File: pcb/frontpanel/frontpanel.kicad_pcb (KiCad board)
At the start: 4 copper layers, 90 parts, among them J1 PICOBLADE_10POS, J2 CONN_01X03, J3 XILINX_JTAG, U1 STM32L431VxIx, U2 TCA6424A

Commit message: Finished initial front panel schematic and design review
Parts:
- added C15: 4.7 uF, azonenberg_pcb:EIA_0603_CAP_NOSILK, F.Cu at (168.8, 51.4)
- added C16: 0.47 uF, azonenberg_pcb:EIA_0402_CAP_NOSILK, F.Cu at (171.7, 51.2)
- added C17: 0.47 uF, azonenberg_pcb:EIA_0402_CAP_NOSILK, F.Cu at (168.3, 53.0)
- added C18: 4.7 uF 25V, azonenberg_pcb:EIA_0805_CAP_NOSILK, F.Cu at (142.6, 62.4)
- added C19: 1 uF 25V, azonenberg_pcb:EIA_0805_CAP_NOSILK, F.Cu at (138.9, 62.4)
- added C20: 1 uF 25V, azonenberg_pcb:EIA_0805_CAP_NOSILK, F.Cu at (138.9, 67.5)
- added C21: 1 uF 25V, azonenberg_pcb:EIA_0805_CAP_NOSILK, F.Cu at (138.9, 65.0)
- added C22: 1 uF 25V, azonenberg_pcb:EIA_0805_CAP_NOSILK, F.Cu at (135.3, 62.4)
- added C23: 1 uF 25V, azonenberg_pcb:EIA_0805_CAP_NOSILK, F.Cu at (135.3, 65.0)
- added C24: 1 uF 25V, azonenberg_pcb:EIA_0805_CAP_NOSILK, F.Cu at (135.3, 67.5)
- added C25: 1 uF 25V, azonenberg_pcb:EIA_0805_CAP_NOSILK, F.Cu at (142.6, 65.0)
- added C26: 0.47 uF, azonenberg_pcb:EIA_0402_CAP_NOSILK, F.Cu at (147.0, 48.0)
- added D33: CTS05S30,L3F, azonenberg_pcb:SOD882, F.Cu at (190.7, 59.0)
- added D34: CTS05S30,L3F, azonenberg_pcb:SOD882, F.Cu at (181.2, 65.7)
- added D35: CTS05S30,L3F, azonenberg_pcb:SOD882, F.Cu at (178.8, 67.2)
- added J4: DISPLAY, azonenberg_pcb:CONN_FFC_0.5MM_1x24_HIROSE_FH34SRJ-24S-0.5SH(50), F.Cu at (108.8, 97.0)
- added L1: TFM322512ALMA100MTAA, azonenberg_pcb:EIA_1210_CAP_NOSILK, F.Cu at (174.9, 66.8)
- added M1: LOGO, azonenberg_pcb:LONGTHING-1200DPI, F.Cu at (169.4, 46.7)
- added M2: LOGO, w_logo:Logo_silk_WEEE_3.4x5mm, F.Cu at (190.2, 46.2)
- added M3: LOGO, w_logo:Logo_silk_OSHW_6x6mm, F.Cu at (186.2, 61.0)
- added M4: LOGO, w_logo:Logo_silk_ROHS_10x5.6mm, F.Cu at (177.8, 61.5)
- added MH1: SCREWHOLE, azonenberg_pcb:MECHANICAL_CLEARANCEHOLE_4_40, B.Cu at (26.0, 108.0)
- added MH2: SCREWHOLE, azonenberg_pcb:MECHANICAL_CLEARANCEHOLE_4_40, F.Cu at (206.0, 89.0)
- added MH3: SCREWHOLE, azonenberg_pcb:MECHANICAL_CLEARANCEHOLE_4_40, B.Cu at (26.0, 89.0)
- added MH4: SCREWHOLE, azonenberg_pcb:MECHANICAL_CLEARANCEHOLE_4_40, F.Cu at (206.0, 108.0)
- added Q1: SSM6N58NU, azonenberg_pcb:DFN_6_0.65MM_2x2MM_GDS, F.Cu at (165.4, 52.3)
- added R38: 0.47, azonenberg_pcb:EIA_0402_RES_NOSILK, F.Cu at (178.7, 65.6)
- added SW1: SWITCH, azonenberg_pcb:SWITCH_RAFI_MICON_5, F.Cu at (160.2, 63.2)
- added SW2: SWITCH, azonenberg_pcb:SWITCH_RAFI_MICON_5, F.Cu at (166.8, 63.2)
- added TP2: CONN_01X08, azonenberg_pcb:CONN_HEADER_2.54MM_1x8, B.Cu at (123.0, 92.0)
- added TP3: CONN_01X08, azonenberg_pcb:CONN_HEADER_2.54MM_1x8, F.Cu at (174.9, 39.6)
- added TP4: U.FL, azonenberg_pcb:CONN_U.FL_TE_1909763-1, F.Cu at (155.0, 43.0)
- added TP5: U.FL, azonenberg_pcb:CONN_U.FL_TE_1909763-1, F.Cu at (160.6, 43.0)
- added U3: AT30TS74_UDFN, azonenberg_pcb:DFN_8_0.5MM_2x3MM_TALL, F.Cu at (202.4, 34.1)
- J1: moved to B.Cu
- moved J1 137.4 mm to (216.0, 99.0), turned to 90 degrees
- moved D20 83.1 mm to (185.0, 109.0)
- moved D17 82.2 mm to (161.0, 109.0)
- moved D19 74.8 mm to (177.0, 109.0)
- moved D18 65.3 mm to (169.0, 109.0)
- moved D16 59.9 mm to (153.0, 109.0)
- moved D15 53.0 mm to (145.0, 109.0)
- moved D22 52.9 mm to (136.7, 35.8)
- moved D24 52.9 mm to (124.4, 53.2)
- moved TP1 52.9 mm to (126.6, 37.2)
- moved C1 52.9 mm to (148.3, 36.9)
- moved C10 52.9 mm to (134.8, 51.4)
- moved C12 52.9 mm to (104.0, 61.4)
- moved C13 52.9 mm to (143.0, 43.0)
- moved C14 52.9 mm to (138.0, 42.4)
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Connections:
- J3 pad 13: /GND -> unconnected-(J3-Pad13)
- U1 pad A1: unconnected-(U1-PadA1) -> /DIRIN_LED_3
- U1 pad A2: unconnected-(U1-PadA2) -> /DIRIN_LED_2
- U1 pad A6: unconnected-(U1-PadA6) -> /UART_TX
- U1 pad A7: unconnected-(U1-PadA7) -> /FRONTPANEL_MISO
- U1 pad B10: unconnected-(U1-PadB10) -> /DPY_SPI_DATA
- U1 pad B11: unconnected-(U1-PadB11) -> /DPY_SPI_SCK
- U1 pad B6: unconnected-(U1-PadB6) -> /UART_RX
- U1 pad D12: unconnected-(U1-PadD12) -> /DIROUT_LED_0
- U1 pad E12: unconnected-(U1-PadE12) -> /DIROUT_LED_1
- U1 pad H12: unconnected-(U1-PadH12) -> /DIROUT_LED_3
- U1 pad J12: unconnected-(U1-PadJ12) -> /DIROUT_LED_2
- U1 pad K12: unconnected-(U1-PadK12) -> /I2C_SCL
- U1 pad L11: unconnected-(U1-PadL11) -> /I2C_SDA
- U1 pad M10: unconnected-(U1-PadM10) -> /FRONTPANEL_SCK
- U1 pad M11: unconnected-(U1-PadM11) -> /DIRIN_LED_1
- U1 pad M12: unconnected-(U1-PadM12) -> /FRONTPANEL_MOSI
- U1 pad M2: unconnected-(U1-PadM2) -> /DPY_BS
- U1 pad M3: unconnected-(U1-PadM3) -> /DPY_SPI_CS_N
- U1 pad M4: unconnected-(U1-PadM4) -> /DPY_BUSY_N
- U1 pad M5: unconnected-(U1-PadM5) -> /FRONTPANEL_CS_N
- U1 pad M6: unconnected-(U1-PadM6) -> /DPY_RST_N
- U1 pad M7: unconnected-(U1-PadM7) -> /DPY_DC
- U1 pad M8: unconnected-(U1-PadM8) -> /TCA_RST_N
- U1 pad M9: unconnected-(U1-PadM9) -> /DIRIN_LED_0
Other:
- board outline added: 200 x 29 mm
- board text added: "Display body outline 59.20 x 29.20 mm"
- board text added: "Front panel has 31mm of height in play for holes etc Board is 29mm high so all good there Standard 5mm clearance from PCB edges should be fine"
- board text added: "MAX WIDTH of total board is 240 mm 225 preferred upper bound Target 200 for initial design with 25 for stretching if necessary"
- board text added: "Visible area 48.548 x 23.712 mm"

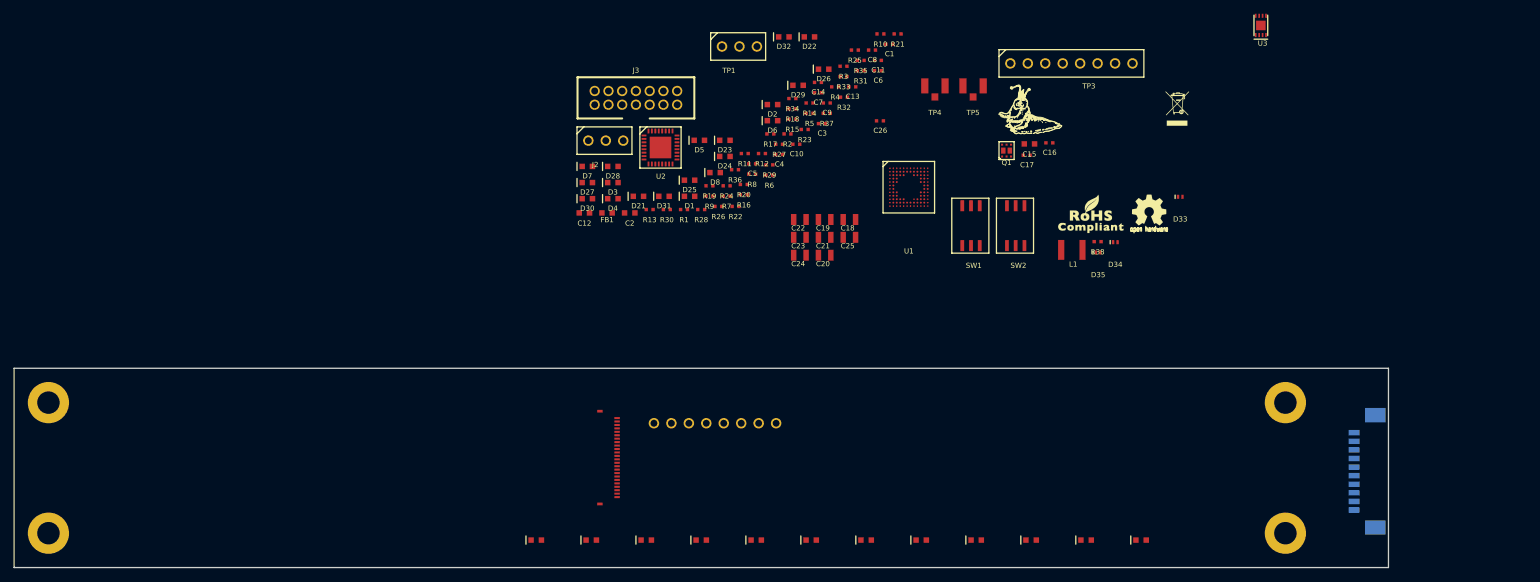
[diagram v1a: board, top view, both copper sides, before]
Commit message: Continued front panel PCB layout
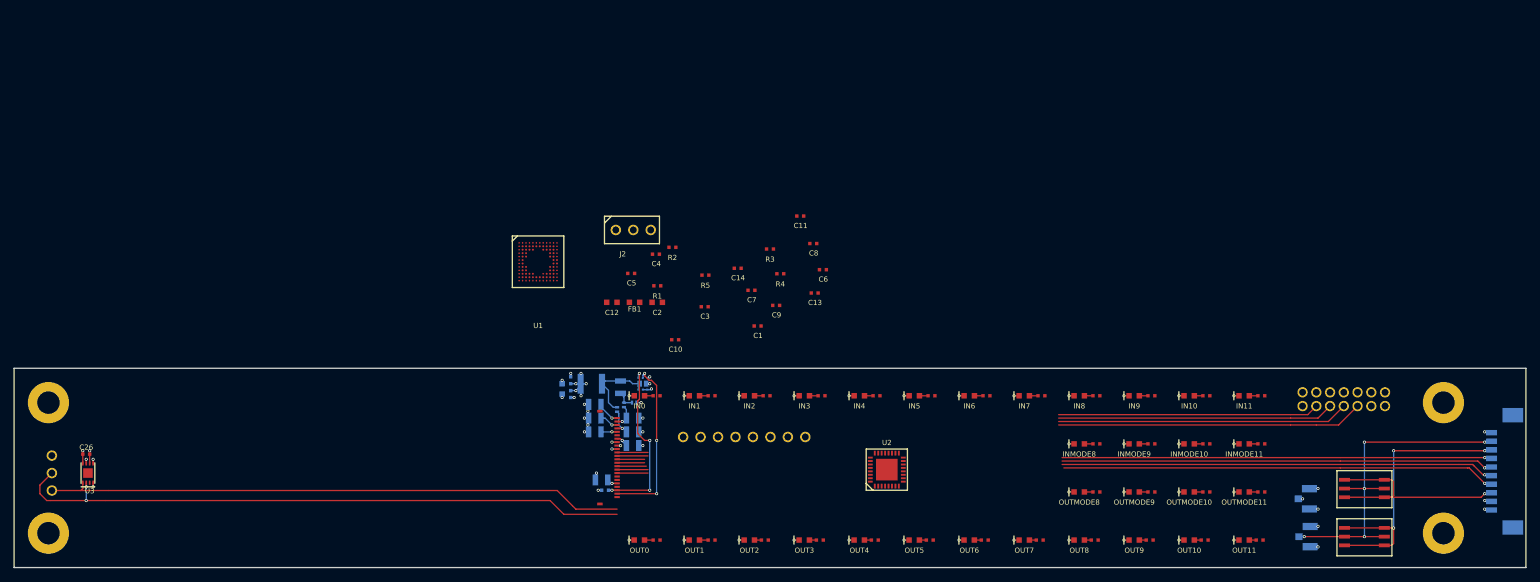
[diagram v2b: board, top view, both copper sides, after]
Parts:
- removed TP3: CONN_01X08, azonenberg_pcb:CONN_HEADER_2.54MM_1x8
- C15, C16, C17, C18, C19, C20, C21, C22, C23, C24, C25, D33, D34, D35, J3, L1, M1, M2, M3, M4, MH2, MH4, Q1, R38, TP1, TP4, TP5: moved to B.Cu
- moved U3 182.7 mm to (31.8, 99.2)
- moved C26 125.3 mm to (31.5, 96.5)
- moved TP1 117.7 mm to (26.5, 99.2), turned to 90 degrees
- moved J3 112.0 mm to (214.5, 88.5)
- moved D4 101.3 mm to (200.0, 102.0)
- moved D7 96.4 mm to (192.0, 95.0)
- moved R13 95.3 mm to (202.5, 95.0), turned to 180 degrees
- moved D3 95.2 mm to (192.0, 102.0)
- moved R25 92.5 mm to (202.2, 109.0), turned to 180 degrees
- moved R9 91.1 mm to (202.5, 102.0), turned to 180 degrees
- moved R24 86.6 mm to (194.2, 109.0), turned to 180 degrees
- moved D8 86.5 mm to (200.0, 95.0)
- moved D32 84.9 mm to (200.0, 88.0)
- moved D33 84.9 mm to (111.2, 89.0), turned to 180 degrees
- moved D30 84.6 mm to (184.0, 88.0)
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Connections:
- C22 pad 2: Net-(C22-Pad2) -> /GND
- C24 pad 2: Net-(C22-Pad2) -> /GND
- C25 pad 2: Net-(C22-Pad2) -> /GND
- TP1 pad 1: /I2C_SCL -> /I2C_SDA
- TP1 pad 2: /I2C_SDA -> /I2C_SCL
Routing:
- net /GND: track 0.00 -> 565.9 mm, vias 0 -> 60
- net /3V3: track 0.00 -> 288.2 mm, vias 0 -> 11
- net /3V3_SB: track 0.00 -> 152.2 mm, vias 0 -> 5
- net /I2C_SCL: track 0.00 -> 91.6 mm, vias 0 -> 2
- net /I2C_SDA: track 0.00 -> 84.6 mm
- net /FRONTPANEL_CS_N: track 0.00 -> 63.2 mm, vias 0 -> 1
- net /FRONTPANEL_MOSI: track 0.00 -> 63.2 mm, vias 0 -> 1
- net /FRONTPANEL_MISO: track 0.00 -> 63.0 mm, vias 0 -> 1
- net /FRONTPANEL_SCK: track 0.00 -> 62.6 mm, vias 0 -> 1
- net /JTAG_TDI: track 0.00 -> 44.6 mm
- net /JTAG_TDO: track 0.00 -> 42.4 mm
- net /SOFT_RST: track 0.00 -> 42.3 mm, vias 0 -> 3
- net /JTAG_TCK: track 0.00 -> 40.2 mm
- net /JTAG_TMS: track 0.00 -> 38.0 mm
- net /SOFT_PWR: track 0.00 -> 32.4 mm, vias 0 -> 1
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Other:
- board size 200 x 29 mm -> 220 x 29 mm
- board text added: "IN0"
- board text added: "IN1"
- board text added: "IN10"
- board text added: "IN11"
- board text added: "IN2"
- board text added: "IN3"
- board text added: "IN4"
- board text added: "IN5"
- board text added: "IN6"
- board text added: "IN7"
- board text added: "IN8"
- board text added: "IN9"
- board text added: "INMODE10"
- board text added: "INMODE11"
- board text added: "INMODE8"
- board text added: "INMODE9"
- board text added: "JTAG"
- board text added: "OUT0"
- board text added: "OUT1"
- board text added: "OUT10"
- board text added: "OUT11"
- board text added: "OUT2"
- board text added: "OUT3"
- board text added: "OUT4"
- board text added: "OUT5"
- board text added: "OUT6"
- board text added: "OUT7"
- board text added: "OUT8"
- board text added: "OUT9"
- board text added: "OUTMODE10"
- board text added: "OUTMODE11"
- board text added: "OUTMODE8"
- board text added: "OUTMODE9"

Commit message: Fully routed front panel ready for layout review
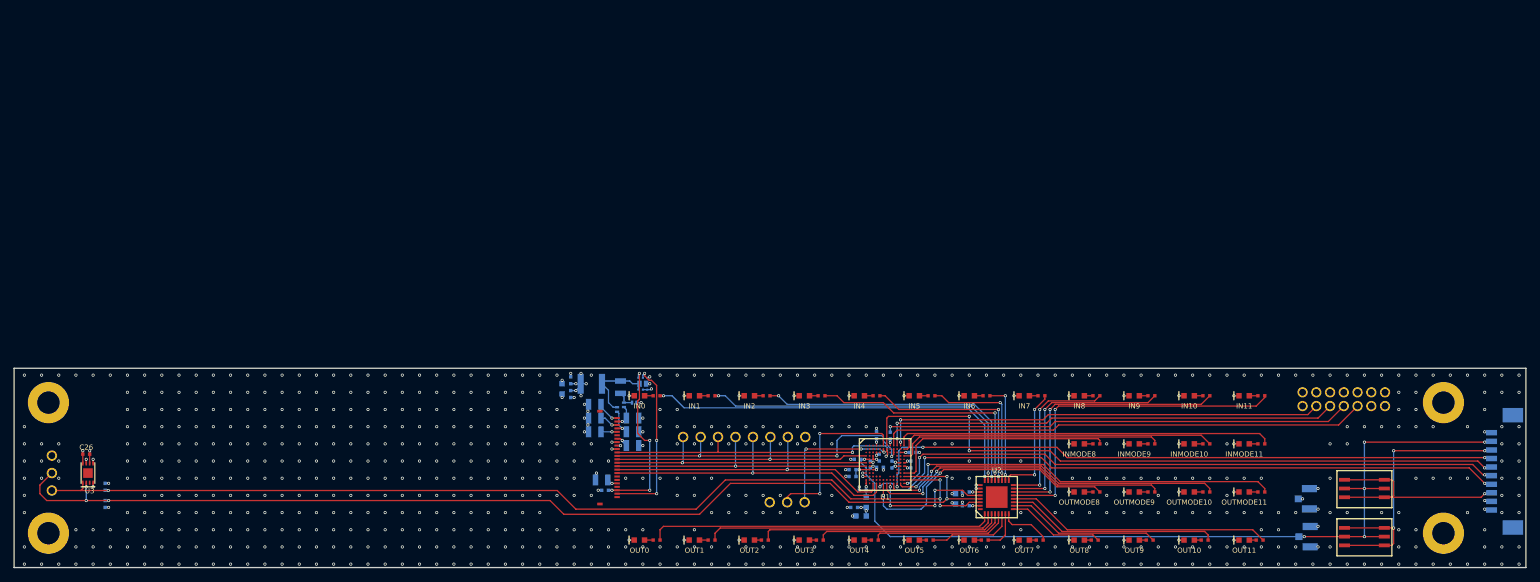
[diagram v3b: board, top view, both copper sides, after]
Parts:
- C1, C10, C11, C12, C13, C14, C2, C3, C4, C5, C6, C7, C8, C9, FB1, J2, R1, R2, R3, R4, R5: moved to B.Cu
- moved R4 103.0 mm to (34.2, 101.2), turned to -90 degrees
- moved R5 93.5 mm to (34.2, 103.8), turned to 90 degrees
- moved U1 58.5 mm to (147.8, 98.0)
- moved C12 57.6 mm to (158.0, 103.0), turned to 90 degrees
- moved C14 46.5 mm to (159.5, 102.0), turned to 180 degrees
- moved C5 46.2 mm to (144.5, 101.8), turned to 180 degrees
- moved J2 45.5 mm to (133.5, 103.5), turned to 180 degrees
- moved FB1 44.5 mm to (145.0, 103.5), turned to -90 degrees
- moved C4 44.0 mm to (146.9, 97.0), turned to -90 degrees
- moved C2 43.0 mm to (144.2, 105.5), turned to 180 degrees
- moved R2 42.4 mm to (143.0, 99.8)
- moved C10 38.8 mm to (151.5, 98.0), turned to 90 degrees
- moved R1 38.6 mm to (146.5, 93.8), turned to 90 degrees
- moved C13 38.0 mm to (159.5, 104.0), turned to 180 degrees
- moved C11 37.6 mm to (145.6, 98.0), turned to 90 degrees
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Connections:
- U1 pad A1: /DIRIN_LED_3 -> unconnected-(U1-PadA1)
- U1 pad A12: unconnected-(U1-PadA12) -> /DIRIN_LED_3
- U1 pad A2: /DIRIN_LED_2 -> unconnected-(U1-PadA2)
- U1 pad B10: /DPY_SPI_DATA -> unconnected-(U1-PadB10)
- U1 pad B11: /DPY_SPI_SCK -> unconnected-(U1-PadB11)
- U1 pad B12: unconnected-(U1-PadB12) -> /DIRIN_LED_2
- U1 pad B7: unconnected-(U1-PadB7) -> /DPY_SPI_DATA
- U1 pad B9: unconnected-(U1-PadB9) -> /DPY_SPI_SCK
- U1 pad C12: unconnected-(U1-PadC12) -> /3V3
- U1 pad C9: unconnected-(U1-PadC9) -> /DPY_SPI_SCK
- U1 pad D1: unconnected-(U1-PadD1) -> /DPY_SPI_CS_N
- U1 pad D12: /DIROUT_LED_0 -> /DIRIN_LED_1
- U1 pad E1: unconnected-(U1-PadE1) -> /3V3_SB
- U1 pad E12: /DIROUT_LED_1 -> unconnected-(U1-PadE12)
- U1 pad F1: unconnected-(U1-PadF1) -> /DPY_DC
- U1 pad G1: unconnected-(U1-PadG1) -> /DPY_RST_N
- U1 pad H1: unconnected-(U1-PadH1) -> /RST_N
- U1 pad H12: /DIROUT_LED_3 -> unconnected-(U1-PadH12)
- U1 pad J12: /DIROUT_LED_2 -> /DIRIN_LED_0
- U1 pad L12: unconnected-(U1-PadL12) -> /I2C_SDA
- U1 pad M11: /DIRIN_LED_1 -> /DIROUT_LED_3
- U1 pad M2: /DPY_BS -> unconnected-(U1-PadM2)
- U1 pad M3: /DPY_SPI_CS_N -> /DPY_BUSY_N
- U1 pad M4: /DPY_BUSY_N -> /DPY_BS
- U1 pad M6: /DPY_RST_N -> /DIROUT_LED_0
- U1 pad M7: /DPY_DC -> /DIROUT_LED_1
- U1 pad M9: /DIRIN_LED_0 -> /DIROUT_LED_2
- U2 pad 1: /TRIGIN_LED_0 -> /TRIGOUT_LED_0
- U2 pad 10: /TRIGIN_LED_9 -> /TRIGOUT_LED_9
- U2 pad 11: /TRIGIN_LED_10 -> /TRIGOUT_LED_10
- U2 pad 12: /TRIGIN_LED_11 -> /TRIGOUT_LED_11
- U2 pad 13: /TRIGOUT_LED_0 -> /TRIGIN_LED_11
- U2 pad 14: /TRIGOUT_LED_1 -> /TRIGIN_LED_10
- U2 pad 15: /TRIGOUT_LED_2 -> /TRIGIN_LED_9
- U2 pad 16: /TRIGOUT_LED_3 -> /TRIGIN_LED_8
- U2 pad 17: /TRIGOUT_LED_4 -> /TRIGIN_LED_7
- U2 pad 18: /TRIGOUT_LED_5 -> /TRIGIN_LED_6
- U2 pad 19: /TRIGOUT_LED_6 -> /TRIGIN_LED_5
- U2 pad 2: /TRIGIN_LED_1 -> /TRIGOUT_LED_1
- U2 pad 20: /TRIGOUT_LED_7 -> /TRIGIN_LED_4
- U2 pad 21: /TRIGOUT_LED_8 -> /TRIGIN_LED_3
- U2 pad 22: /TRIGOUT_LED_9 -> /TRIGIN_LED_2
- U2 pad 23: /TRIGOUT_LED_10 -> /TRIGIN_LED_1
- U2 pad 24: /TRIGOUT_LED_11 -> /TRIGIN_LED_0
- U2 pad 3: /TRIGIN_LED_2 -> /TRIGOUT_LED_2
- U2 pad 4: /TRIGIN_LED_3 -> /TRIGOUT_LED_3
- U2 pad 5: /TRIGIN_LED_4 -> /TRIGOUT_LED_4
- U2 pad 6: /TRIGIN_LED_5 -> /TRIGOUT_LED_5
- U2 pad 7: /TRIGIN_LED_6 -> /TRIGOUT_LED_6
- U2 pad 8: /TRIGIN_LED_7 -> /TRIGOUT_LED_7
- U2 pad 9: /TRIGIN_LED_8 -> /TRIGOUT_LED_8
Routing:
- net /GND: track 565.9 -> 642.0 mm, vias 60 -> 721
- net /I2C_SCL: track 91.6 -> 157.6 mm, vias 2 -> 5
- net /I2C_SDA: track 84.6 -> 150.6 mm, vias 0 -> 4
- net /DIROUT_LED_3: track 0.00 -> 57.5 mm, vias 0 -> 2
- net /TRIGIN_LED_0: track 0.00 -> 57.1 mm, vias 0 -> 2
- net /DIRIN_LED_3: track 0.00 -> 55.0 mm
- net /DIROUT_LED_2: track 0.00 -> 50.7 mm, vias 0 -> 2
- net /TRIGOUT_LED_0: track 0.00 -> 50.4 mm
- net /TRIGIN_LED_11: track 0.00 -> 50.1 mm, vias 0 -> 2
- net /TRIGIN_LED_1: track 0.00 -> 49.8 mm, vias 0 -> 2
- net /3V3: track 288.2 -> 336.3 mm, vias 11 -> 25
- net /DIRIN_LED_2: track 0.00 -> 46.4 mm
- net /DIROUT_LED_1: track 0.00 -> 44.2 mm, vias 0 -> 2
- net /DPY_SPI_SCK: track 4.50 -> 48.7 mm, vias 0 -> 3
- net /TRIGOUT_LED_1: track 0.00 -> 42.7 mm
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- added copper zone on In2.Cu, net /3V3
- added copper zone on In1.Cu, net /GND
- added copper zone on In2.Cu, net /GND
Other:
- board text added: "3V3"
- board text added: "3V3_SB"
- board text added: "BS"
- board text added: "BUSY#"
- board text added: "CS#"
- board text added: "DATA"
- board text added: "DC"
- board text added: "DISPLAY"
- board text added: "GND"
- board text added: "I2C"
- board text added: "MAX WIDTH of total board is 240 mm 225 preferred upper bound"
- board text added: "RST#"
- board text added: "RX"
- board text added: "SCK"
- board text added: "SCL"
- board text added: "SDA"
- board text added: "TX"
- board text added: "UART"
- board text removed: "MAX WIDTH of total board is 240 mm 225 preferred upper bound Target 200 for initial design with 25 for stretching if necessary"

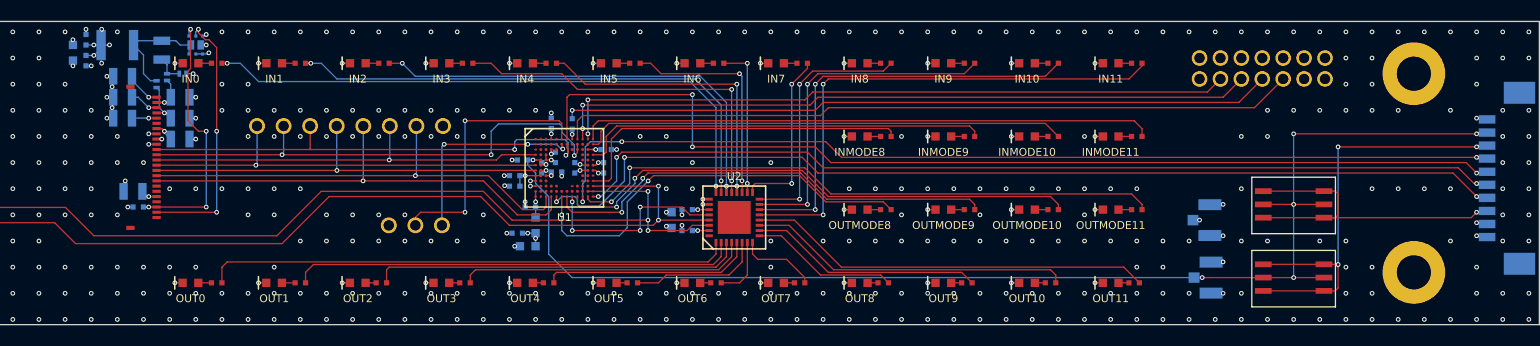
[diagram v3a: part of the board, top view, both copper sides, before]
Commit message: Hopefully-final front panel PCB layout after layout review, pending final exports and mechanical fit check on enclosure
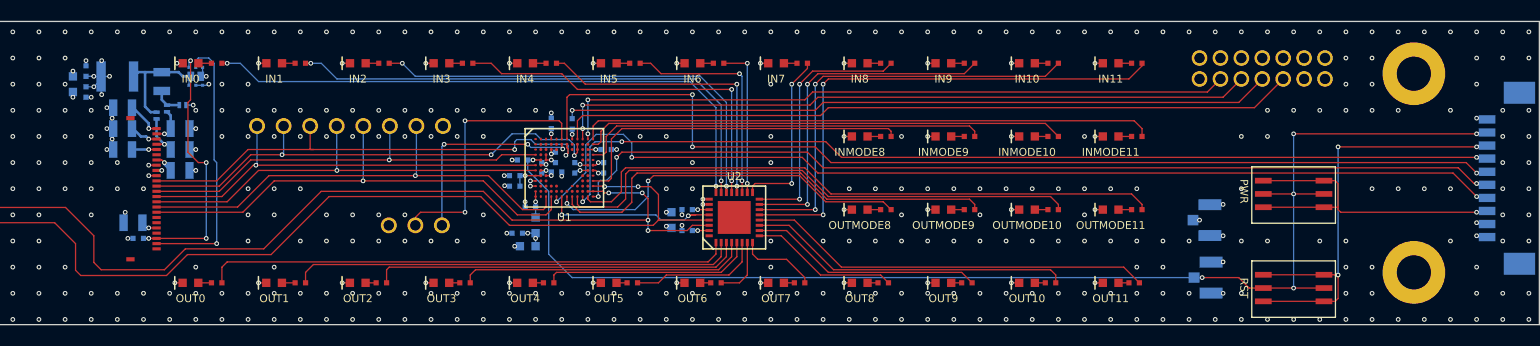
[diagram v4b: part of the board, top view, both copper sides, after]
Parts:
- moved C15 3.00 mm to (100.8, 90.0)
- moved C16 3.00 mm to (102.0, 90.8)
- moved C17 3.00 mm to (102.0, 88.8)
- moved C18 3.00 mm to (109.2, 89.8)
- moved C19 3.00 mm to (111.0, 94.2)
- moved C20 3.00 mm to (111.0, 96.2)
- moved C21 3.00 mm to (106.5, 103.2)
- moved C22 3.00 mm to (105.5, 96.2)
- moved C23 3.00 mm to (111.0, 98.2)
- moved C24 3.00 mm to (105.5, 92.2)
- moved C25 3.00 mm to (105.5, 94.2)
- moved D33 3.00 mm to (111.2, 92.0)
- moved D34 3.00 mm to (109.8, 92.3)
- moved D35 3.00 mm to (108.8, 93.0)
- moved J4 3.00 mm to (108.8, 100.0)
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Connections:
- U1 pad M6: /DIROUT_LED_0 -> /TCA_RST_N
- U1 pad M7: /DIROUT_LED_1 -> /DIROUT_LED_0
- U1 pad M8: /TCA_RST_N -> /DIROUT_LED_1
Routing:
- net /GND: track 642.0 -> 654.2 mm
- net /3V3: track 336.3 -> 344.9 mm
- net /DIROUT_LED_0: track 40.1 -> 35.5 mm
- net /I2C_SDA: track 150.6 -> 154.3 mm, vias 4 -> 5
- net /I2C_SCL: track 157.6 -> 161.2 mm
- net /TCA_RST_N: track 18.9 -> 16.8 mm, vias 4 -> 2
- net /FRONTPANEL_CS_N: track 95.2 -> 97.1 mm
- net /3V3_SB: track 124.3 -> 125.7 mm
- net /DPY_SPI_DATA: track 45.0 -> 46.4 mm
- net /DPY_SPI_CS_N: track 39.7 -> 41.0 mm
- net /DPY_RST_N: track 40.5 -> 41.8 mm
- net /DPY_DC: track 40.0 -> 41.3 mm
- net /DPY_BUSY_N: track 44.5 -> 45.7 mm
- net /DPY_BS: track 45.8 -> 47.1 mm
- net /DPY_SPI_SCK: track 48.7 -> 47.5 mm
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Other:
- board text added: "PWR"
- board text added: "RST"
- board text added: "Trigger Crossbar Front Panel A. Zonenberg / 2024-03-11 / v0.1 S/N:"
